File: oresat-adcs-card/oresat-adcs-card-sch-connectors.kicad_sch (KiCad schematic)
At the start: 14 parts

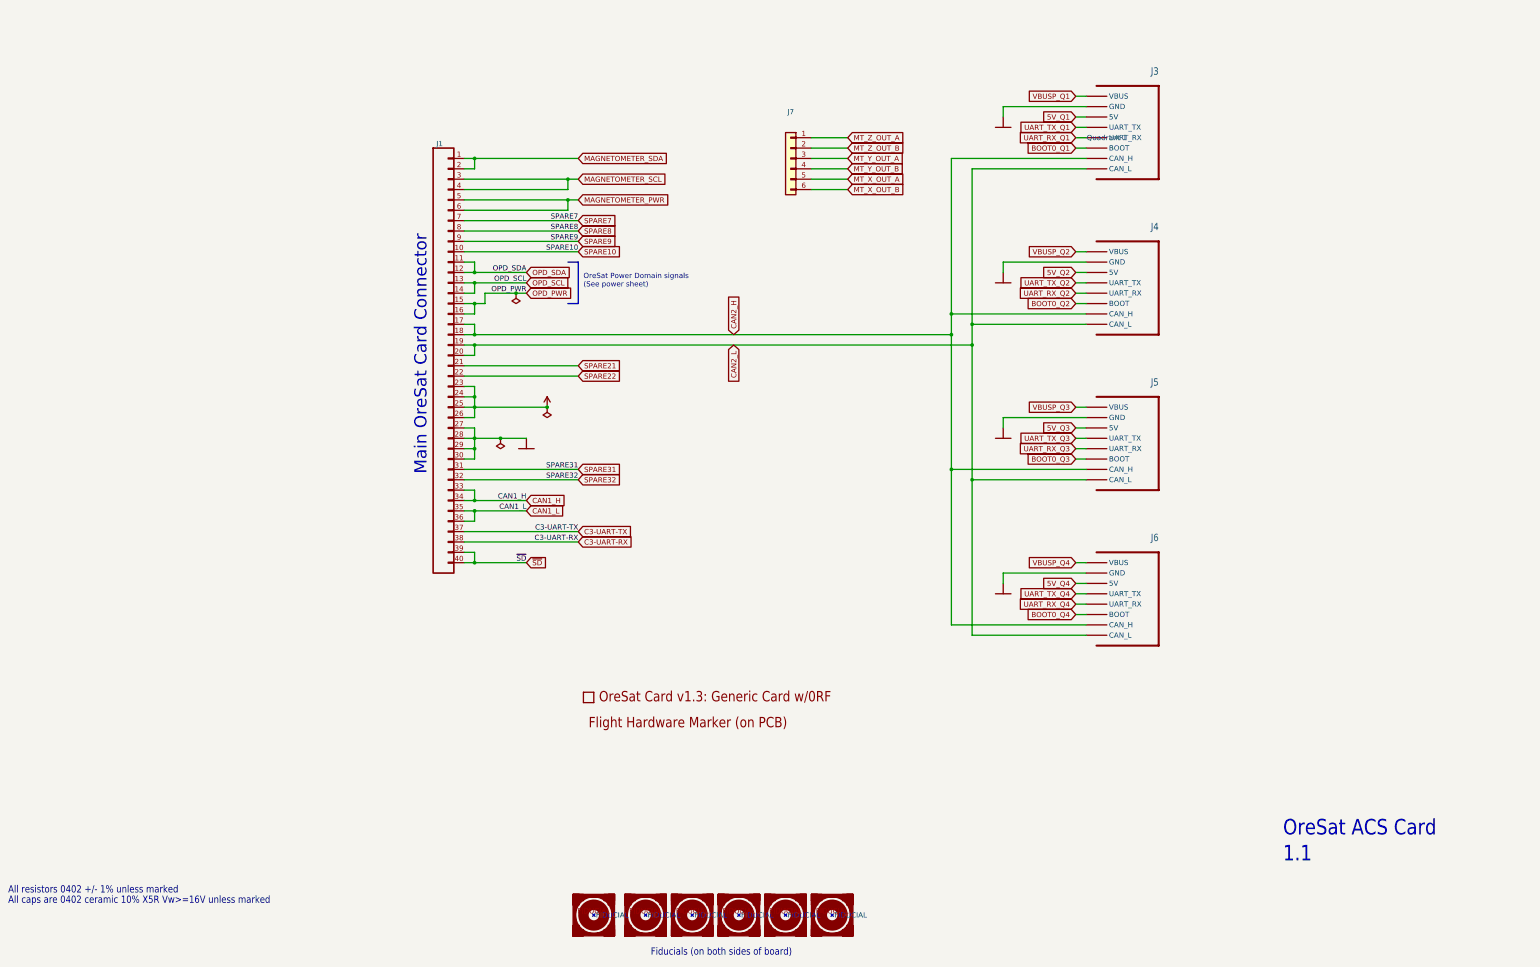
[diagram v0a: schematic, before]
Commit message: Design review changes
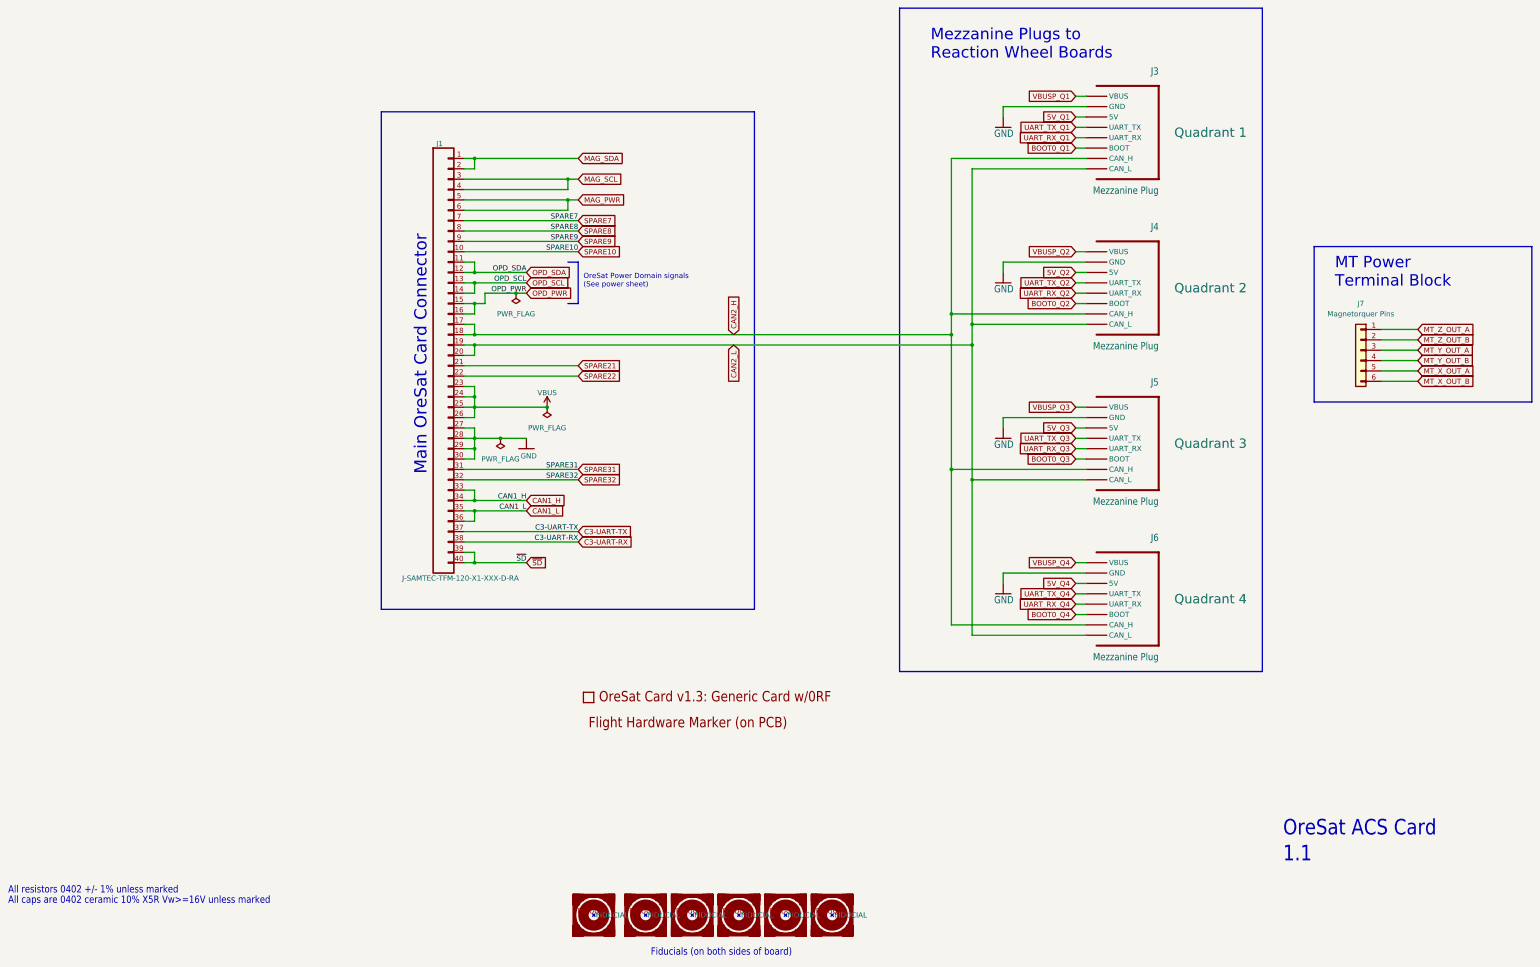
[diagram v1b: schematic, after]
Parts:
- FIDUCIAL1, FIDUCIAL2, FIDUCIAL3, FIDUCIAL4, FIDUCIAL5, FIDUCIAL6: value (none) -> FIDUCIAL-1.0X2.0; footprint (none) -> oresat-acs-card:FIDUCIAL-1.0X2.0
- J1: value (none) -> J-SAMTEC-TFM-120-X1-XXX-D-RA; footprint (none) -> oresat-footprints:J-SAMTEC-TFM-120-X1-XXX-D-RA
- J3, J4, J5, J6: value (none) -> Mezzanine Plug; footprint (none) -> oresat-footprints:J-Molex-555600307
- J7: value (none) -> Magnetorquer Pins; footprint (none) -> oresat-footprints:J-Wurth-691243100006
- PCB1: renamed from PCB?; value (none) -> ORESAT-CARD-V1.3-GENERIC-0RF; footprint (none) -> oresat-acs-card:ORESAT-CARD-V1.3-GENERIC-0RF
- U$1: renamed from U$?; value (none) -> FLIGHMARKERNEW; footprint (none) -> oresat-acs-card:FLIGHTMARKER_NEW_BOARDS
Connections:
- net MAGNETOMETER_PWR renamed MAG_PWR
- net MAGNETOMETER_SCL renamed MAG_SCL
- net MAGNETOMETER_SDA renamed MAG_SDA
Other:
- note added: "MT Power Terminal Block"
- note added: "Mezzanine Plugs to Reaction Wheel Boards"
- moved on the sheet: J7

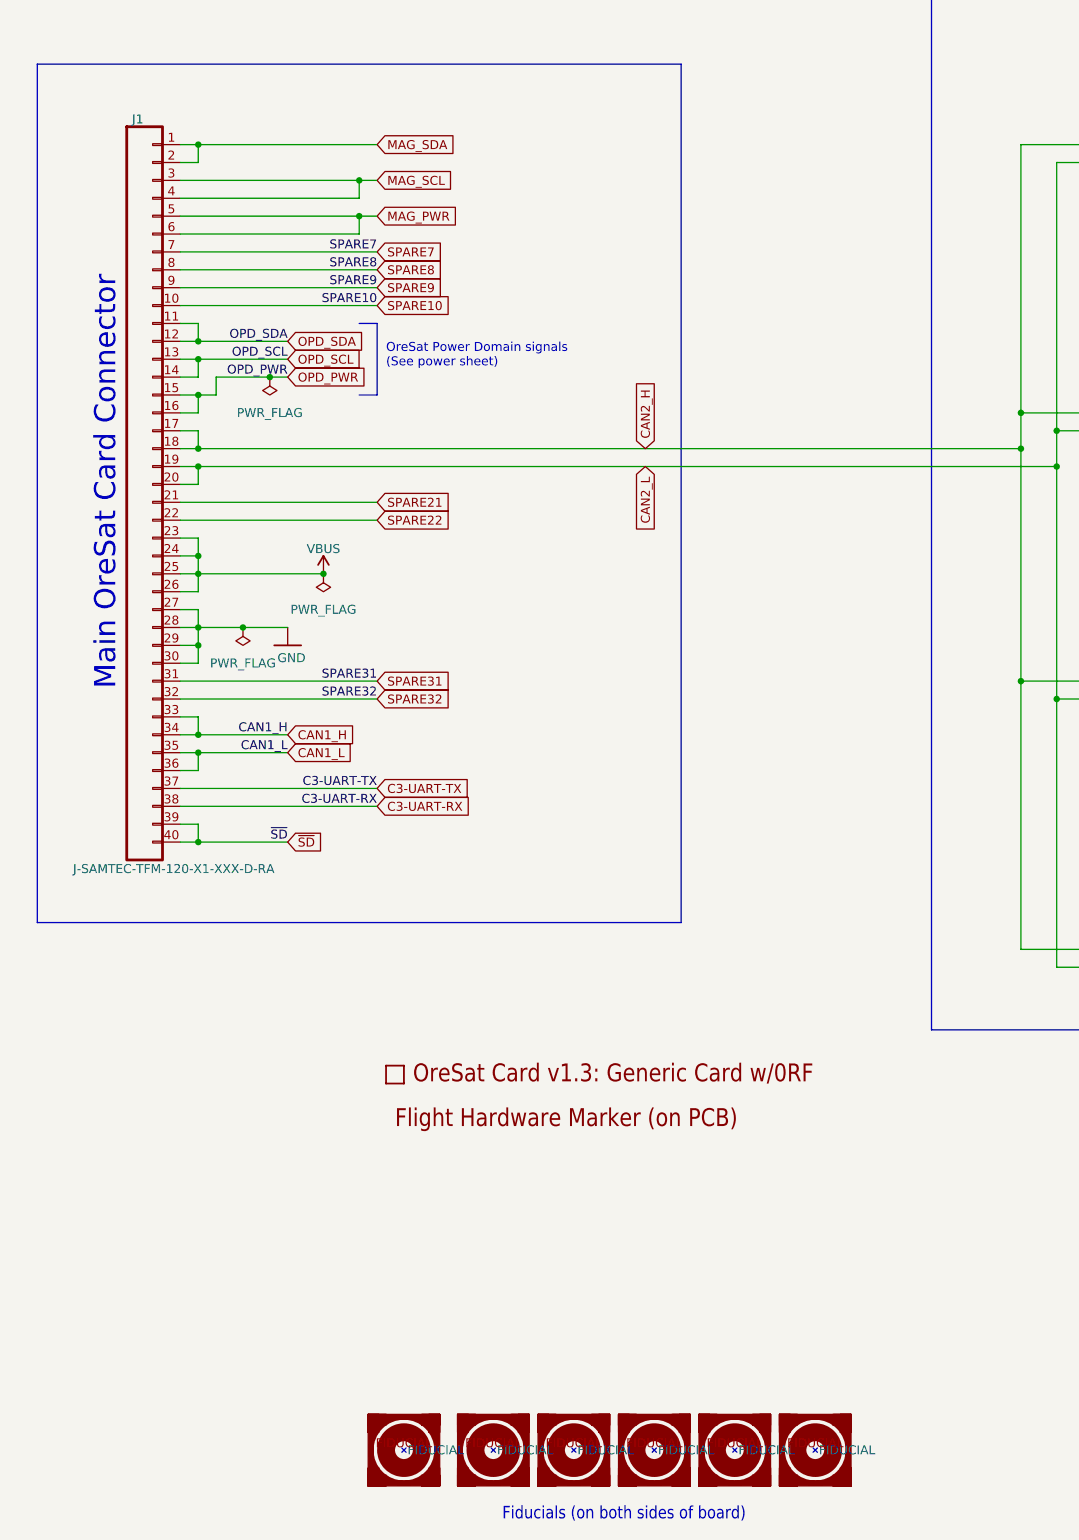
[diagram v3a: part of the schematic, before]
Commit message: Updated ADCS card and fixed library issues
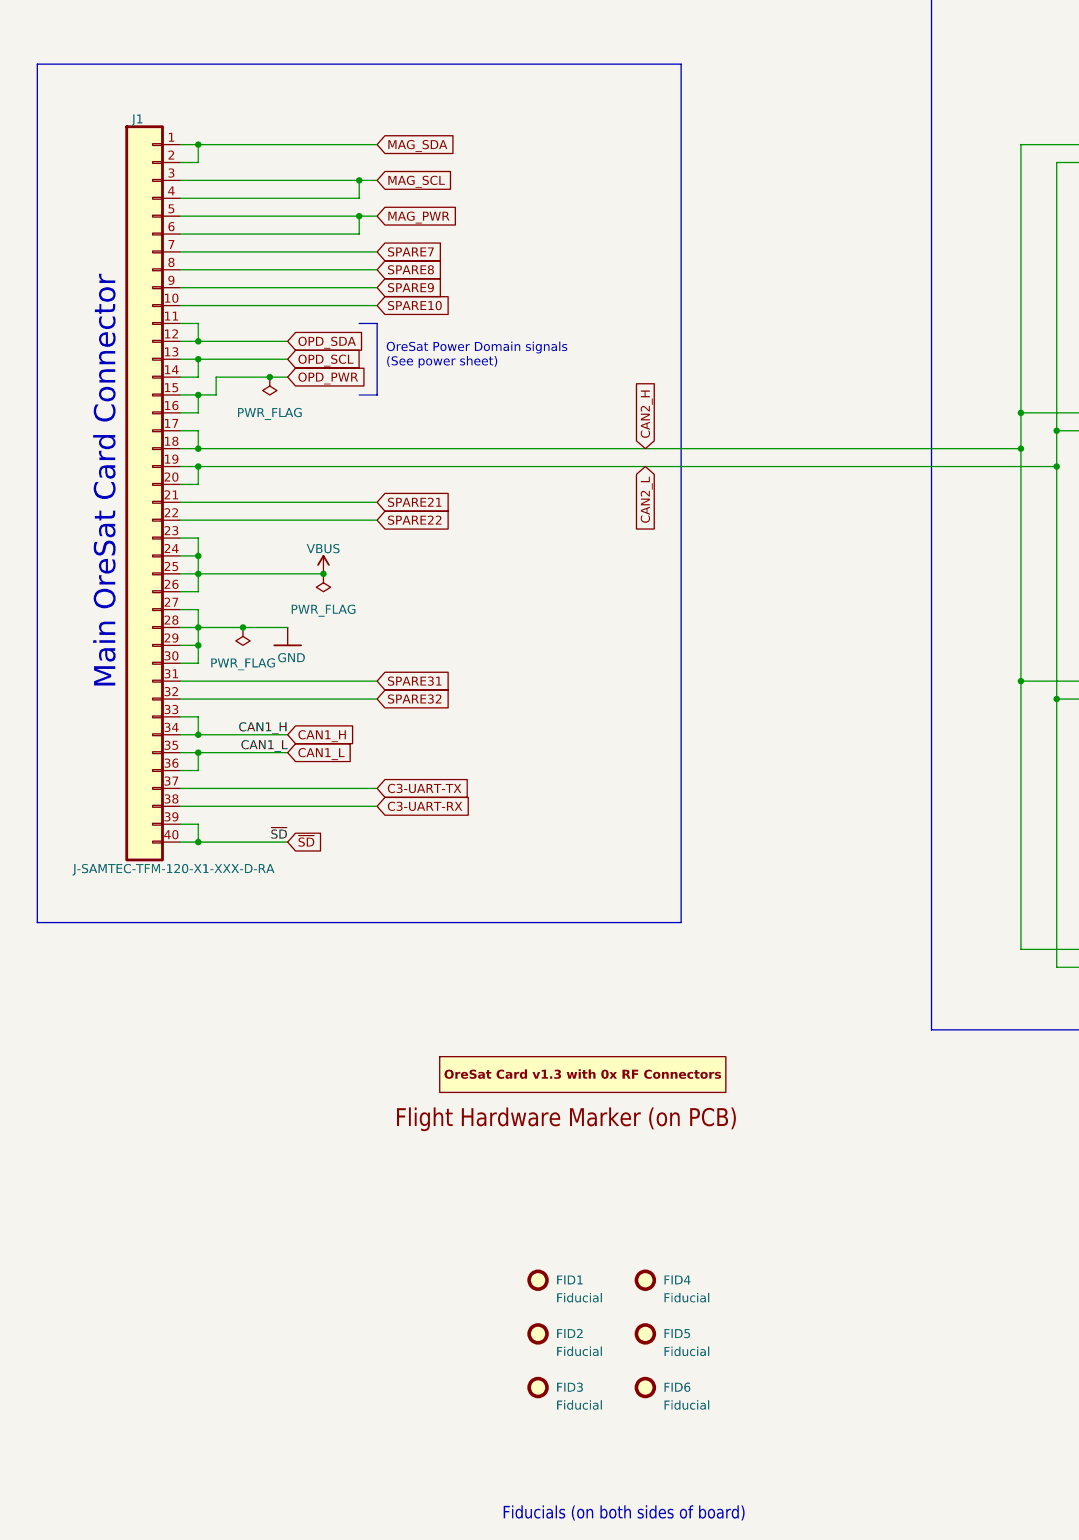
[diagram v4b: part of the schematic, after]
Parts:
- FID1: renamed from FIDUCIAL1; value FIDUCIAL-1.0X2.0 -> Fiducial; footprint oresat-acs-card:FIDUCIAL-1.0X2.0 -> Fiducial:Fiducial_1mm_Mask2mm; symbol oresat-acs-card-eagle-import:FIDUCIAL-1.0X2.0 -> Mechanical:Fiducial; now in the parts list
- FID2: renamed from FIDUCIAL2; value FIDUCIAL-1.0X2.0 -> Fiducial; footprint oresat-acs-card:FIDUCIAL-1.0X2.0 -> Fiducial:Fiducial_1mm_Mask2mm; symbol oresat-acs-card-eagle-import:FIDUCIAL-1.0X2.0 -> Mechanical:Fiducial; now in the parts list
- FID3: renamed from FIDUCIAL3; value FIDUCIAL-1.0X2.0 -> Fiducial; footprint oresat-acs-card:FIDUCIAL-1.0X2.0 -> Fiducial:Fiducial_1mm_Mask2mm; symbol oresat-acs-card-eagle-import:FIDUCIAL-1.0X2.0 -> Mechanical:Fiducial; now in the parts list
- FID4: renamed from FIDUCIAL4; value FIDUCIAL-1.0X2.0 -> Fiducial; footprint oresat-acs-card:FIDUCIAL-1.0X2.0 -> Fiducial:Fiducial_1mm_Mask2mm; symbol oresat-acs-card-eagle-import:FIDUCIAL-1.0X2.0 -> Mechanical:Fiducial; now in the parts list
- FID5: renamed from FIDUCIAL5; value FIDUCIAL-1.0X2.0 -> Fiducial; footprint oresat-acs-card:FIDUCIAL-1.0X2.0 -> Fiducial:Fiducial_1mm_Mask2mm; symbol oresat-acs-card-eagle-import:FIDUCIAL-1.0X2.0 -> Mechanical:Fiducial; now in the parts list
- FID6: renamed from FIDUCIAL6; value FIDUCIAL-1.0X2.0 -> Fiducial; footprint oresat-acs-card:FIDUCIAL-1.0X2.0 -> Fiducial:Fiducial_1mm_Mask2mm; symbol oresat-acs-card-eagle-import:FIDUCIAL-1.0X2.0 -> Mechanical:Fiducial; now in the parts list
- J1: footprint oresat-footprints:J-SAMTEC-TFM-120-X1-XXX-D-RA -> oresat-connectors:J-SAMTEC-TFM-120-X1-XXX-D-RA; symbol J-SAMTEC-TFM-120-01-L-D-RA-oresat-backplane-connector:J-SAMTEC-TFM-120-01-L-D-RA -> oresat-connectors:J-SAMTEC-TFM-120-01-L-D-RA
- J3, J4, J5, J6: footprint oresat-footprints:J-Molex-555600307 -> oresat-connectors:J-Molex-555600307; symbol J-Molex-555600307-mezzanine-plug:555600307 -> oresat-connectors:Mezzanine Plug
- J7: footprint oresat-footprints:J-Wurth-691243100006 -> oresat-connectors:J-Wurth-691243100006
- PCB1: footprint oresat-acs-card:ORESAT-CARD-V1.3-GENERIC-0RF -> oresat-pcbs:ORESAT-CARD-V1.3-0RF; symbol oresat-acs-card-eagle-import:ORESAT-CARD-V1.3-GENERIC-0RF -> oresat-pcbs:ORESAT-CARD-V1.3-0RF; now in the parts list
